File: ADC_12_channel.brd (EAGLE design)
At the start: 160 x 127 mm, 163 parts, among them K1 691131710003, K2 691101710002, K3 691101710002, K4 691101710002, K5 691101710002, K6 691101710002, K7 691101710002, K8 691101710002, K9 691101710002, U1 AD7864ASZ-1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

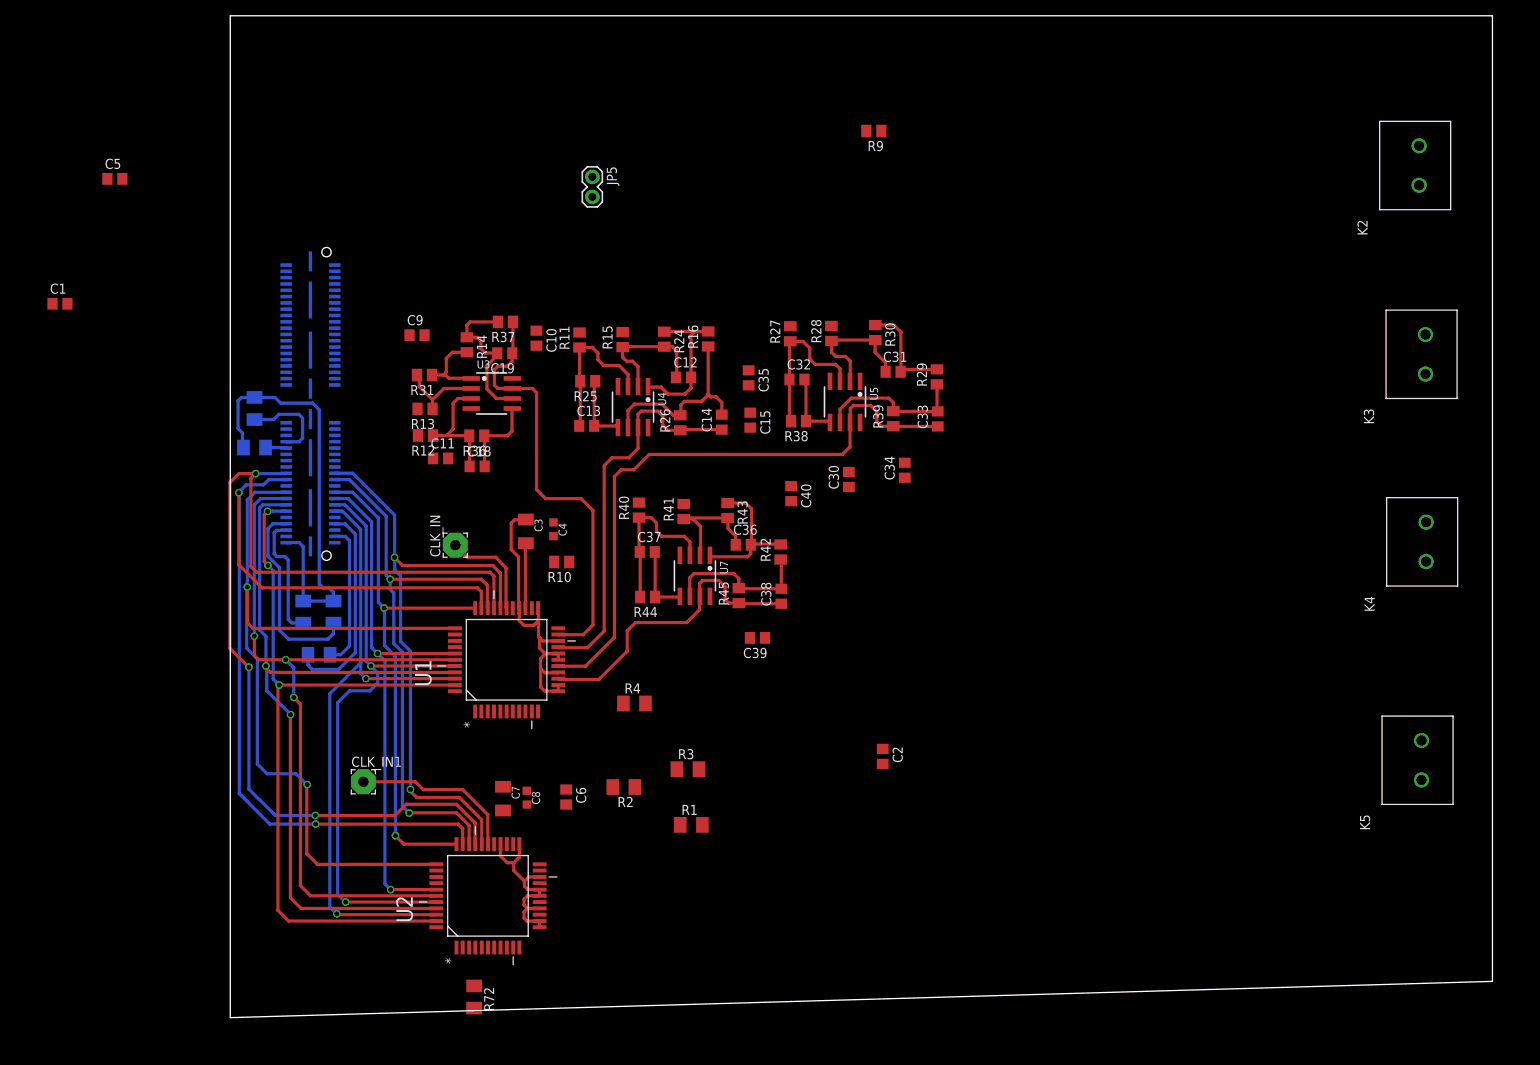
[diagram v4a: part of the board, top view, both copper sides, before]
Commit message: End of session Commit
Moved ADC-1 to further right
Layed remaining Data bit
Layed busy bit
Removed int/ext clock signal resistor
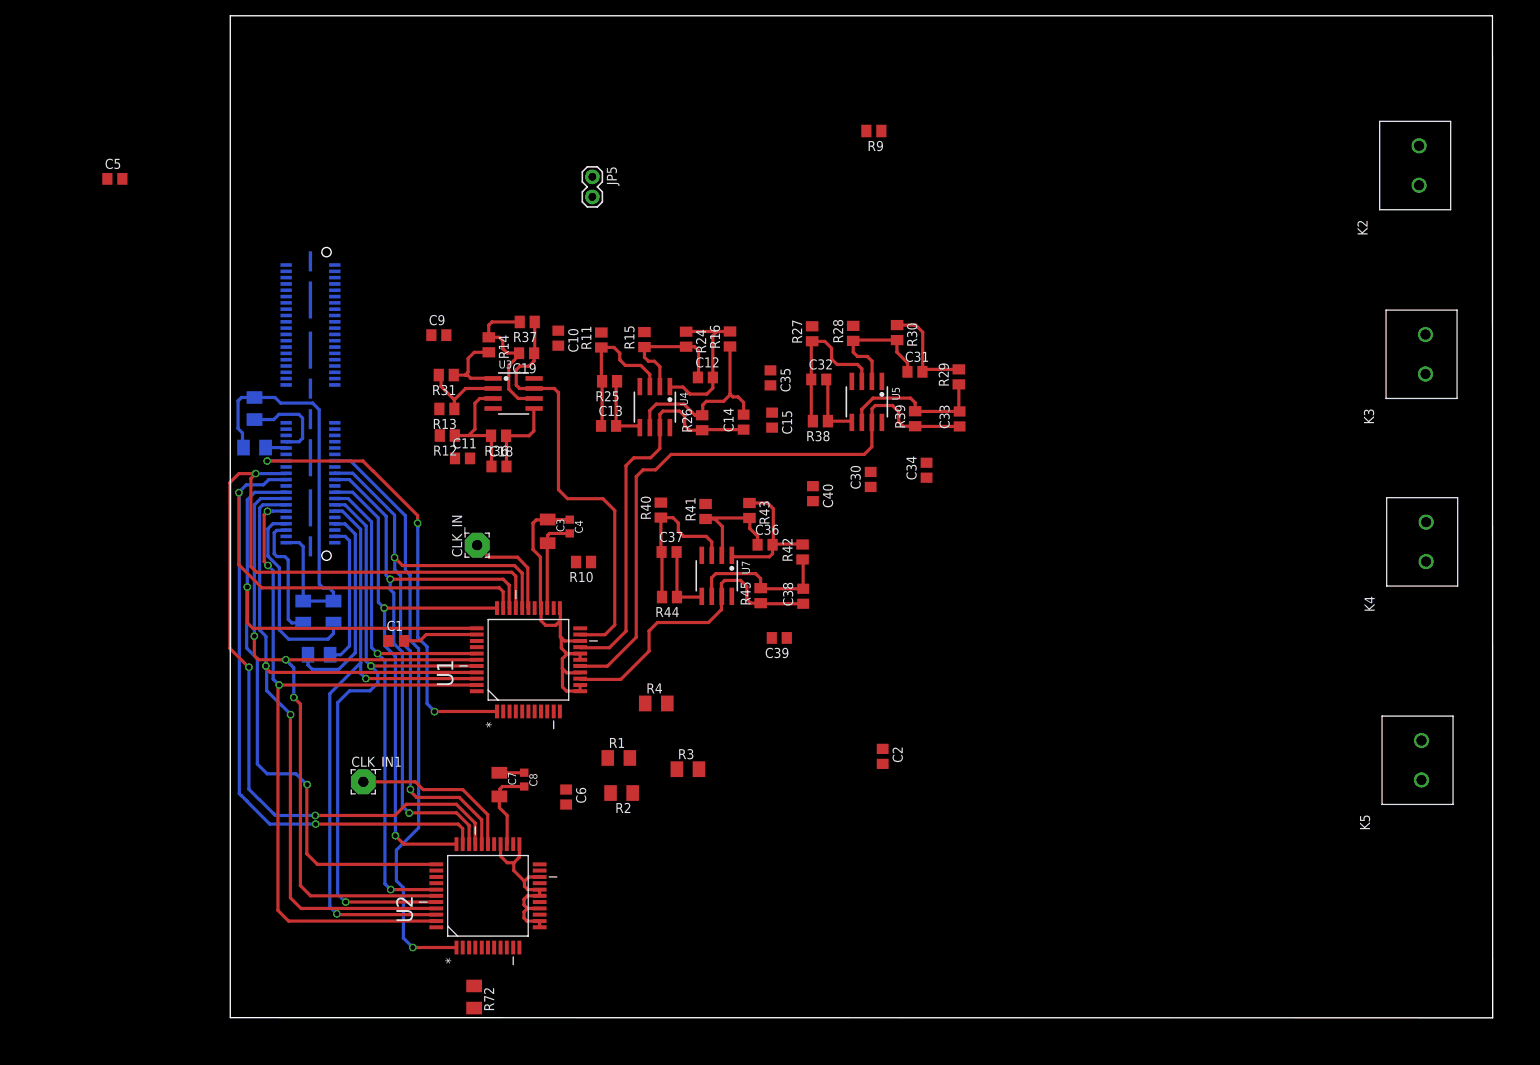
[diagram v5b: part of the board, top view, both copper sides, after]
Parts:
- moved C1 60.4 mm to (21.1, 20.8)
- moved R1 12.5 mm to (49.3, 5.92)
- moved C15 2.77 mm to (68.7, 48.7)
- moved C32 2.77 mm to (74.6, 53.9)
- moved C33 2.77 mm to (92.5, 48.9)
- moved C34 2.77 mm to (88.3, 42.4)
- moved C38 2.77 mm to (72.6, 26.4)
- moved C39 2.77 mm to (69.6, 21.1)
- moved C40 2.77 mm to (73.9, 39.4)
- moved R15 2.77 mm to (52.5, 59.0)
- moved R27 2.77 mm to (73.8, 59.7)
- moved R39 2.77 mm to (86.8, 48.9)
- moved R42 2.77 mm to (72.5, 32.0)
- moved R43 2.77 mm to (65.8, 37.3)
- moved R45 2.77 mm to (67.2, 26.5)
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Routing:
- net N$52: track 0.00 -> 74.8 mm, vias 0 -> 1
- net N$50: track 0.00 -> 58.6 mm, vias 0 -> 3
- net VDD: track 8.25 -> 22.8 mm
- net DVDD: track 0.00 -> 9.55 mm
- net AGND: track 101.7 -> 107.6 mm
- net N$7: track 129.2 -> 132.0 mm
- net N$8: track 79.5 -> 82.3 mm
- net N$4: track 96.3 -> 99.0 mm
- net N$3: track 98.1 -> 100.8 mm
- net N$12: track 77.9 -> 80.7 mm
- net N$10: track 67.8 -> 70.5 mm
- net N$1: track 96.9 -> 99.7 mm
- net N$9: track 69.1 -> 71.9 mm
- net N$6: track 120.4 -> 123.1 mm
- net N$5: track 103.6 -> 106.3 mm
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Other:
- outline, holes or cut-outs redrawn

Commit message: Commit before major revision (A restore point!) rearranging ADC input opamps to a borld position
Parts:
- moved C52 233.7 mm to (61.5, -14.2), turned to 90 degrees
- moved R58 230.2 mm to (65.8, -4.32), turned to 90 degrees
- moved C51 227.2 mm to (61.9, -19.9), turned to 90 degrees
- moved R46 225.7 mm to (65.0, 3.91), turned to 180 degrees
- moved U9 221.0 mm to (68.6, -10.6), turned to 90 degrees
- moved C57 217.7 mm to (89.2, -15.3), turned to 90 degrees
- moved U6 217.6 mm to (71.9, 6.78), turned to 180 degrees
- moved C50 216.7 mm to (71.2, -4.32), turned to 270 degrees
- moved R56 216.6 mm to (67.1, -16.9), turned to 180 degrees
- moved C17 215.4 mm to (64.7, 8.97)
- moved R64 215.0 mm to (93.7, -5.38), turned to 270 degrees
- moved C42 213.1 mm to (77.5, -0.03), turned to 180 degrees
- moved R57 210.4 mm to (77.3, -23.3), turned to 180 degrees
- moved C49 208.0 mm to (71.3, -19.9), turned to 270 degrees
- moved C41 207.3 mm to (78.0, 4.75), turned to 90 degrees
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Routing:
- net N$61: track 0.00 -> 19.8 mm
- net N$64: track 0.00 -> 18.0 mm
- net N$62: track 0.00 -> 15.0 mm
- net ADC5: track 0.00 -> 13.5 mm
- net AGND: track 107.6 -> 120.4 mm
- net N$63: track 0.00 -> 4.85 mm
- net VDD: track 22.8 -> 24.3 mm

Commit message: Restore pint - 2 Moved ADC chip connected the two resistors
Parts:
- added R71: 0, resistor:M1206
- moved JP5 9.81 mm to (20.2, -24.0)
- moved C12 5.89 mm to (66.1, 54.2)
- moved C14 5.89 mm to (71.0, 48.5)
- moved C16 5.89 mm to (84.3, 9.80)
- moved C30 5.89 mm to (74.5, 59.7)
- moved C31 5.89 mm to (92.7, 54.9)
- moved C35 5.89 mm to (74.4, 54.1)
- moved C36 5.89 mm to (73.7, 33.0)
- moved C41 5.89 mm to (83.9, 4.78)
- moved C43 5.89 mm to (72.3, 15.3)
- moved C44 5.89 mm to (110.3, 18.3)
- moved R28 5.89 mm to (84.9, 59.8)
- moved R29 5.89 mm to (98.2, 54.3)
- moved R30 5.89 mm to (90.4, 59.9)
- moved R33 5.89 mm to (83.3, 15.0)
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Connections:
- new net N$47: C20.+, C59.1, R17.1, U$1.1
- net VCC_12+: no longer C20.+, C59.1, R17.1, U$1.1
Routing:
- net DVDD: track 9.55 -> 53.5 mm, vias 0 -> 2
- net DGND: track 0.00 -> 17.0 mm
- net N$50: track 58.6 -> 64.5 mm
- net N$9: track 71.9 -> 77.8 mm
- net N$8: track 82.3 -> 88.2 mm
- net N$27: track 84.0 -> 89.9 mm
- net N$12: track 80.7 -> 86.5 mm
- net N$10: track 70.5 -> 76.4 mm
- net N$30: track 76.2 -> 82.1 mm
- net N$1: track 99.7 -> 105.6 mm
- net N$3: track 100.8 -> 106.7 mm
- net N$6: track 123.1 -> 129.0 mm
- net N$7: track 132.0 -> 137.9 mm
- net N$4: track 99.0 -> 103.5 mm
- net N$5: track 106.3 -> 109.4 mm

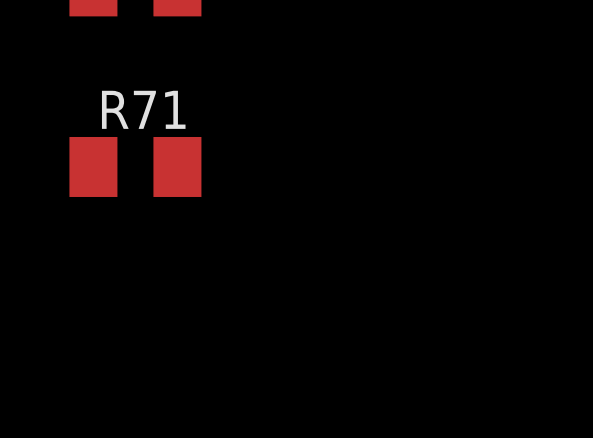
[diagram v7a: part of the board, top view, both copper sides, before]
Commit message: Added a voltage divider for 3V supply corrected the VDD and AVDD mess-up
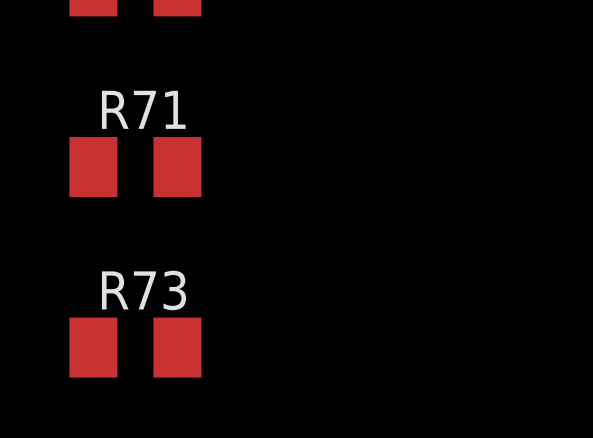
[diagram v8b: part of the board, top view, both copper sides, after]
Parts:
- added R73: 0, resistor:M1206
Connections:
- removed net N$47: C20.+, C59.1, R17.1, U$1.1
- new net 5V: C28.+, R71.1, R73.2, U12.3
- net GND2: now also R73.1
- net VCC_12+: now also C20.+, C59.1, R17.1, R71.2, U$1.1; no longer C28.+, U12.3
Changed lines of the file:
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@@
 <element name="R72" library="resistor" package="M1206" value="0" x="47.4218" y="-19.2532"/>
 <element name="R71" library="resistor" package="M1206" value="0" x="-144.5768" y="-210.566"/>
+<element name="R73" library="resistor" package="M1206" value="0" x="-144.5768" y="-216.5858"/>
 </elements>
 <signals>
@@
 <wire x1="46.369" y1="34.4056" x2="46.1264" y2="34.163" width="0.4064" layer="1"/>
 <wire x1="46.1264" y1="34.163" x2="46.1264" y2="33.171" width="0.4064" layer="1"/>
+<wire x1="35.052" y1="-5.0038" x2="35.1282" y2="-5.0038" width="0.4064" layer="1"/>
+<wire x1="35.1282" y1="-5.0038" x2="35.1282" y2="2.8688" width="0.4064" layer="1"/>
 <wire x1="48.9204" y1="34.4056" x2="80.6348" y2="85.3948" width="0" layer="19" extent="1-1"/>
 <wire x1="49.723" y1="30.7848" x2="48.9204" y2="34.4056" width="0" layer="19" extent="1-1"/>
-<wire x1="64.1858" y1="5.204" x2="46.0756" y2="24.9428" width="0" layer="19" extent="1-1"/>
-<wire x1="53.6448" y1="5.2548" x2="64.1858" y2="5.204" width="0" layer="19" extent="1-1"/>
+<wire x1="41.7576" y1="34.544" x2="46.1264" y2="34.163" width="0" layer="19" extent="1-1"/>
+<wire x1="61.6428" y1="19.812" x2="49.723" y2="30.7848" width="0" layer="19" extent="1-1"/>
+<wire x1="58.9534" y1="5.3056" x2="61.6428" y2="19.812" width="0" layer="19" extent="1-1"/>
+<wire x1="64.1858" y1="5.204" x2="58.9534" y2="5.3056" width="0" layer="19" extent="1-1"/>
+<wire x1="53.6448" y1="5.2548" x2="58.9534" y2="5.3056" width="0" layer="19" extent="1-1"/>
 <wire x1="48.4378" y1="5.3056" x2="53.6448" y2="5.2548" width="0" layer="19" extent="1-1"/>
-<wire x1="58.9534" y1="5.3056" x2="53.6448" y2="5.2548" width="0" layer="19" extent="1-1"/>
 <wire x1="38.2778" y1="4.1288" x2="48.4378" y2="5.3056" width="0" layer="19" extent="1-1"/>
-<wire x1="41.7576" y1="34.544" x2="46.1264" y2="34.163" width="0" layer="19" extent="1-1"/>
-<wire x1="61.6428" y1="19.812" x2="41.7576" y2="34.544" width="0" layer="19" extent="1-1"/>
-<wire x1="45.5422" y1="-25.1054" x2="61.6428" y2="19.812" width="0" layer="19" extent="1-1"/>
-<wire x1="40.259" y1="-25.0292" x2="45.5422" y2="-25.1054" width="0" layer="19" extent="1-1"/>
+<wire x1="40.259" y1="-25.0292" x2="35.1282" y2="-5.0038" width="0" layer="19" extent="1-1"/>
 <wire x1="35.0774" y1="-25.715" x2="40.259" y2="-25.0292" width="0" layer="19" extent="1-1"/>
-<wire x1="35.052" y1="-5.0038" x2="35.1282" y2="-5.0038" width="0.4064" layer="1"/>
-<wire x1="35.1282" y1="-5.0038" x2="35.1282" y2="2.8688" width="0.4064" layer="1"/>
+<wire x1="45.5422" y1="-25.1054" x2="40.259" y2="-25.0292" width="0" layer="19" extent="1-1"/>
 </signal>
 <signal name="N$16">
@@
 </signal>
 <signal name="VCC_12+">
-<contactref element="C28" pad="+"/>
 <contactref element="U3" pad="8"/>
 <contactref element="C10" pad="2"/>
@@
 <contactref element="U10" pad="8"/>
 <contactref element="C57" pad="2"/>
-<contactref element="U12" pad="3"/>
-<wire x1="-141.4018" y1="-195.0212" x2="-50.8" y2="-97.79" width="0" layer="19" extent="1-1"/>
-<wire x1="61.5188" y1="-13.274" x2="-50.8" y2="-97.79" width="0" layer="19" extent="1-1"/>
+<contactref element="C20" pad="+"/>
+<contactref element="U$1" pad="1"/>
+<contactref element="R17" pad="1"/>
+<contactref element="R71" pad="2"/>
+<contactref element="C59" pad="1"/>
+<wire x1="-62.23" y1="-83.82" x2="-58.572" y2="-127" width="0" layer="19" extent="1-1"/>
+<wire x1="-128.1532" y1="-162.6202" x2="-58.572" y2="-127" width="0" layer="19" extent="1-1"/>
+<wire x1="-138.3132" y1="-178.1302" x2="-128.1532" y2="-162.6202" width="0" layer="19" extent="1-1"/>
+<wire x1="-143.1768" y1="-210.566" x2="-138.3132" y2="-178.1302" width="0" layer="19" extent="1-1"/>
+<wire x1="61.5188" y1="-13.274" x2="-62.23" y2="-83.82" width="0" layer="19" extent="1-1"/>
 <wire x1="65.9546" y1="-12.4968" x2="61.5188" y2="-13.274" width="0" layer="19" extent="1-1"/>
 <wire x1="82.4382" y1="0" x2="65.9546" y2="-12.4968" width="0" layer="19" extent="1-1"/>
 <wire x1="79.6798" y1="4.2072" x2="82.4382" y2="0" width="0" layer="19" extent="1-1"/>
+<wire x1="89.1794" y1="-14.3408" x2="82.4382" y2="0" width="0" layer="19" extent="1-1"/>
+<wire x1="93.8438" y1="-13.843" x2="89.1794" y2="-14.3408" width="0" layer="19" extent="1-1"/>
 <wire x1="74.5388" y1="21.1582" x2="79.6798" y2="4.2072" width="0" layer="19" extent="1-1"/>
 <wire x1="69.469" y1="26.4322" x2="74.5388" y2="21.1582" width="0" layer="19" extent="1-1"/>
-<wire x1="89.1794" y1="-14.3408" x2="82.4382" y2="0" width="0" layer="19" extent="1-1"/>
-<wire x1="93.8438" y1="-13.843" x2="89.1794" y2="-14.3408" width="0" layer="19" extent="1-1"/>
 <wire x1="109.032" y1="0.3302" x2="93.8438" y2="-13.843" width="0" layer="19" extent="1-1"/>
 <wire x1="103.8606" y1="4.9184" x2="109.032" y2="0.3302" width="0" layer="19" extent="1-1"/>
@@
 <contactref element="C22" pad="1"/>
 <contactref element="U12" pad="1"/>
+<contactref element="R73" pad="1"/>
 <wire x1="-67.79" y1="-137.16" x2="-73.508" y2="-138.43" width="0" layer="19" extent="1-1"/>
 <wire x1="-70.89" y1="-128.27" x2="-67.79" y2="-137.16" width="0" layer="19" extent="1-1"/>
@@
 <wire x1="-138.3132" y1="-184.4802" x2="-136.4132" y2="-178.1302" width="0" layer="19" extent="1-1"/>
 <wire x1="-146.0246" y1="-195.0212" x2="-138.3132" y2="-184.4802" width="0" layer="19" extent="1-1"/>
+<wire x1="-145.9768" y1="-216.5858" x2="-146.0246" y2="-195.0212" width="0" layer="19" extent="1-1"/>
 </signal>
 <signal name="N$38">
@@
 <wire x1="-145.0594" y1="-199.8726" x2="-143.1768" y2="-204.5462" width="0" layer="19" extent="1-1"/>
 </signal>
-<signal name="N$47">
-<contactref element="C20" pad="+"/>
-<contactref element="C59" pad="1"/>
-<contactref element="U$1" pad="1"/>
-<contactref element="R17" pad="1"/>
-<wire x1="-62.23" y1="-83.82" x2="-58.572" y2="-127" width="0" layer="19" extent="1-1"/>
-<wire x1="-128.1532" y1="-162.6202" x2="-58.572" y2="-127" width="0" layer="19" extent="1-1"/>
-<wire x1="-138.3132" y1="-178.1302" x2="-128.1532" y2="-162.6202" width="0" layer="19" extent="1-1"/>
+<signal name="5V">
+<contactref element="C28" pad="+"/>
+<contactref element="U12" pad="3"/>
+<contactref element="R73" pad="2"/>
+<contactref element="R71" pad="1"/>
+<wire x1="-141.4018" y1="-195.0212" x2="-50.8" y2="-97.79" width="0" layer="19" extent="1-1"/>
+<wire x1="-145.9768" y1="-210.566" x2="-141.4018" y2="-195.0212" width="0" layer="19" extent="1-1"/>
+<wire x1="-143.1768" y1="-216.5858" x2="-145.9768" y2="-210.566" width="0" layer="19" extent="1-1"/>
 </signal>
 </signals>
